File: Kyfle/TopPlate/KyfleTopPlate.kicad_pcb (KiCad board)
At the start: 2 copper layers, 160.8 x 138.4 mm, 39 parts, among them SW2 KEY_SWITCH, SW2 PRO MICRO

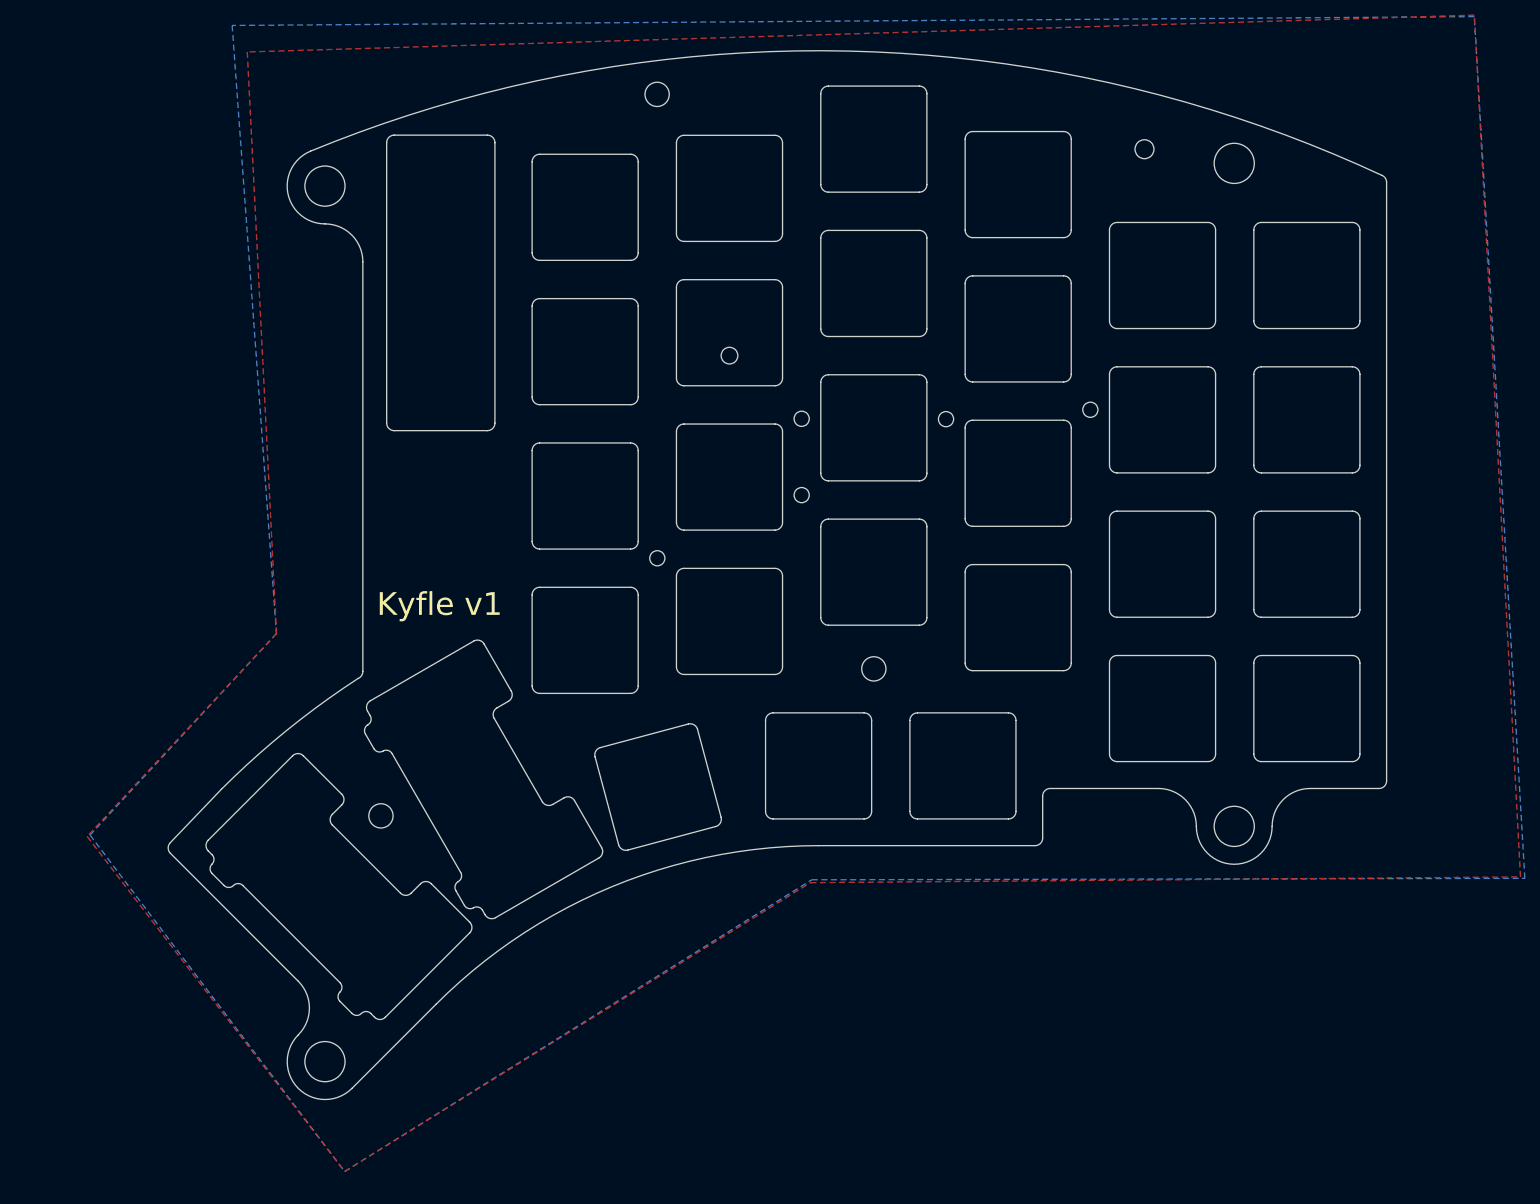
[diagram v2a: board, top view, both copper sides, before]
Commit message: Experimentation with different fastening solutions. Not great.
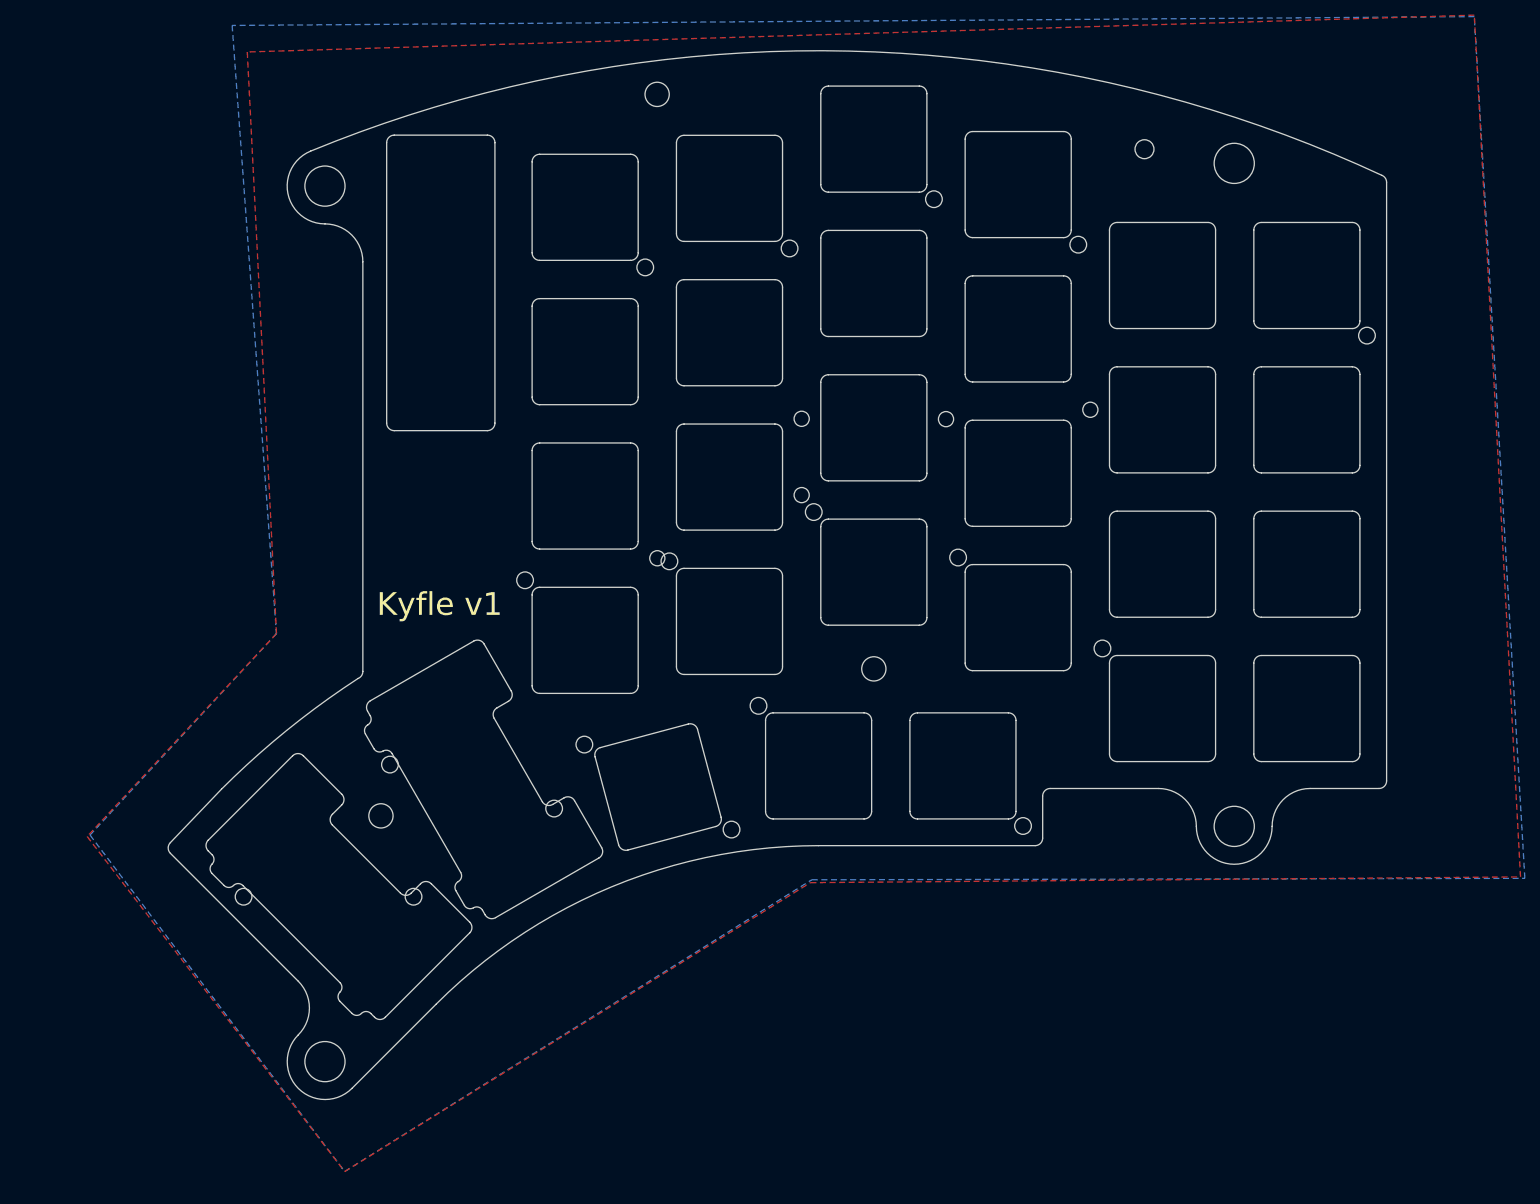
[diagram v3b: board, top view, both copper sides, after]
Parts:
- removed the REF** at (150.0, 64.0)
- added REF**: MountingHole_2.2mm_M2_ISO14580, SofleChocTop:M2_with_washer, F.Cu at (153.8, 110.2)
- added REF**: MountingHole_2.2mm_M2_ISO14580, SofleChocTop:M2_with_washer, F.Cu at (177.0, 43.3)
- added REF**: MountingHole_2.2mm_M2_ISO14580, SofleChocTop:M2_with_washer, F.Cu at (85.9, 135.4)
- added REF**: MountingHole_2.2mm_M2_ISO14580, SofleChocTop:M2_with_washer, F.Cu at (161.1, 84.6)
- added REF**: MountingHole_2.2mm_M2_ISO14580, SofleChocTop:M2_with_washer, F.Cu at (188.7, 126.0)
- added REF**: MountingHole_2.2mm_M2_ISO14580, SofleChocTop:M2_with_washer, F.Cu at (157.9, 49.8)
- added REF**: MountingHole_2.2mm_M2_ISO14580, SofleChocTop:M2_with_washer, F.Cu at (142.1, 91.1)
- added REF**: MountingHole_2.2mm_M2_ISO14580, SofleChocTop:M2_with_washer, F.Cu at (105.2, 117.9)
- added REF**: MountingHole_2.2mm_M2_ISO14580, SofleChocTop:M2_with_washer, F.Cu at (138.9, 52.3)
- added REF**: MountingHole_2.2mm_M2_ISO14580, SofleChocTop:M2_with_washer, F.Cu at (130.8, 115.3)
- added REF**: MountingHole_2.2mm_M2_ISO14580, SofleChocTop:M2_with_washer, F.Cu at (108.3, 135.4)
- added REF**: MountingHole_2.2mm_M2_ISO14580, SofleChocTop:M2_with_washer, F.Cu at (180.2, 90.6)
- added REF**: MountingHole_2.2mm_M2_ISO14580, SofleChocTop:M2_with_washer, F.Cu at (234.1, 61.3)
- added REF**: MountingHole_2.2mm_M2_ISO14580, SofleChocTop:M2_with_washer, F.Cu at (126.9, 123.7)
- added REF**: MountingHole_2.2mm_M2_ISO14580, SofleChocTop:M2_with_washer, F.Cu at (199.2, 102.6)
- added REF**: MountingHole_2.2mm_M2_ISO14580, SofleChocTop:M2_with_washer, F.Cu at (150.3, 126.5)
- added REF**: MountingHole_2.2mm_M2_ISO14580, SofleChocTop:M2_with_washer, F.Cu at (123.0, 93.6)
- added REF**: MountingHole_2.2mm_M2_ISO14580, SofleChocTop:M2_with_washer, F.Cu at (196.0, 49.3)

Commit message: Settled on a solution to fix the PCB
It will be hold by the bottom plate only.
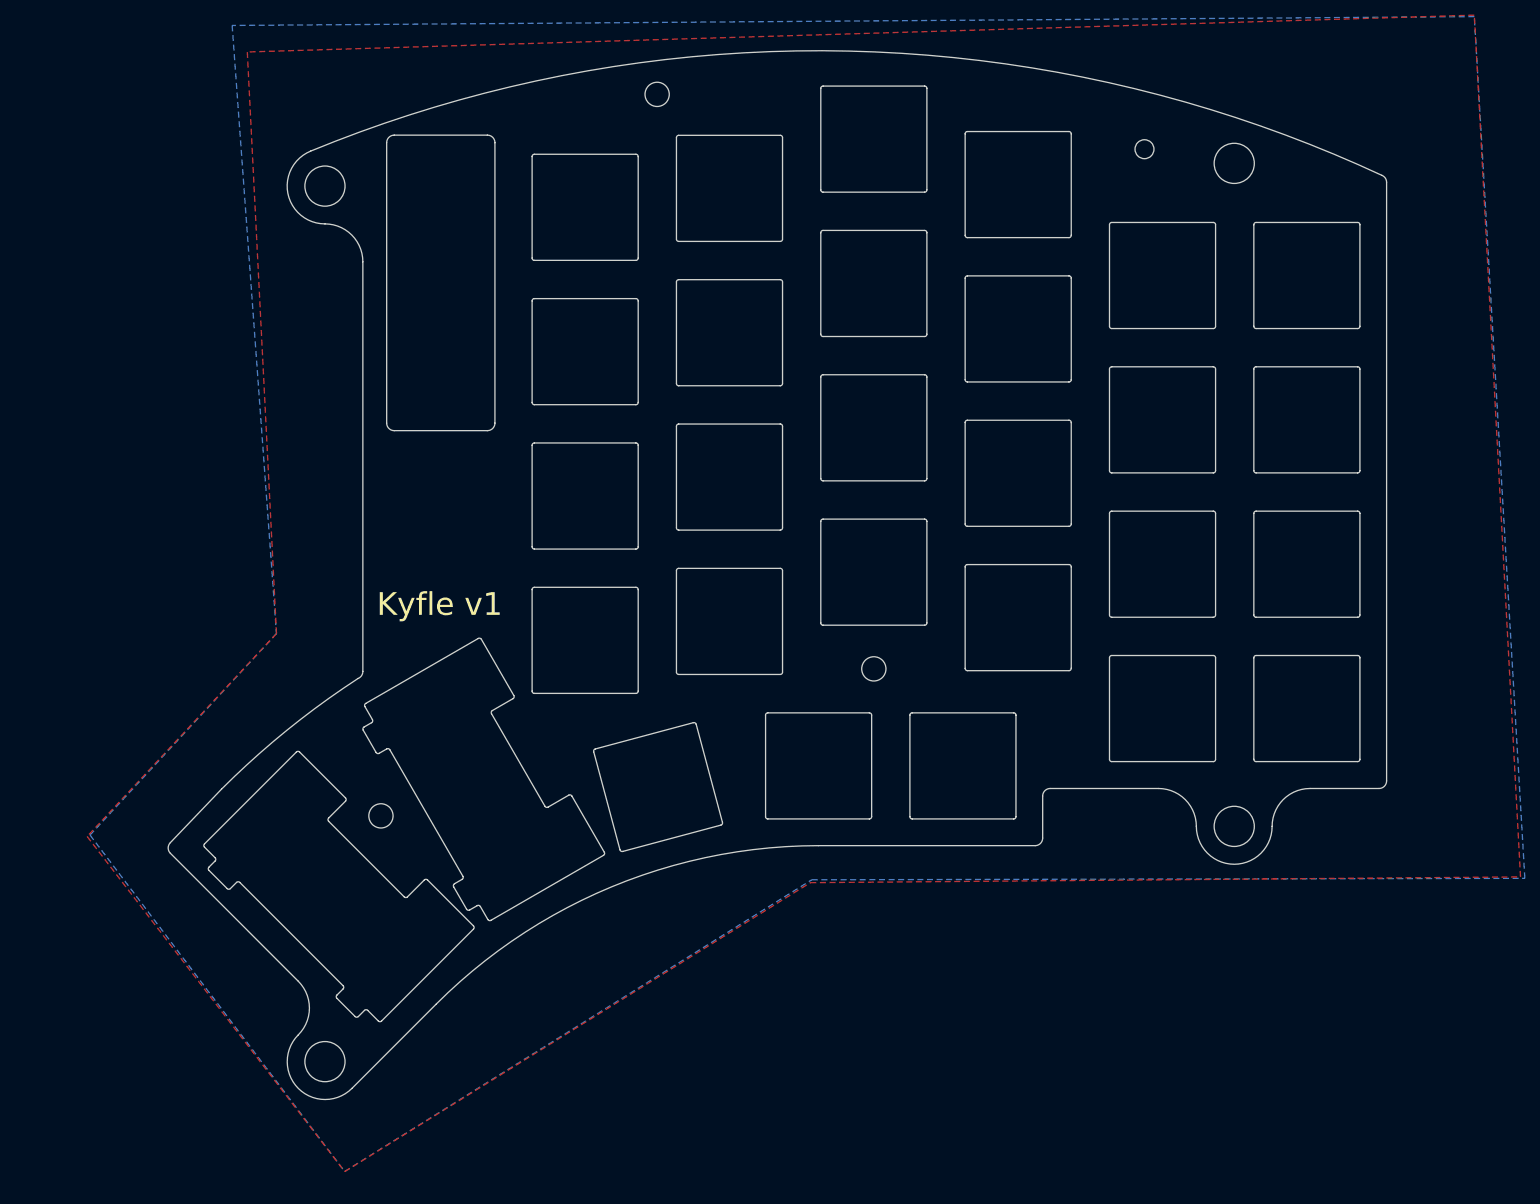
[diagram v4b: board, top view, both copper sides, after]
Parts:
- removed the REF** at (153.8, 110.2)
- removed the REF** at (177.0, 43.3)
- removed the REF** at (85.9, 135.4)
- removed the REF** at (161.1, 84.6)
- removed the REF** at (188.7, 126.0)
- removed the REF** at (157.9, 49.8)
- removed the REF** at (142.1, 91.1)
- removed the REF** at (105.2, 117.9)
- removed the REF** at (138.9, 52.3)
- removed the REF** at (130.8, 115.3)
- removed the REF** at (108.3, 135.4)
- removed the REF** at (180.2, 90.6)
- removed the REF** at (234.1, 61.3)
- removed the REF** at (126.9, 123.7)
- removed the REF** at (199.2, 102.6)
- removed the REF** at (150.3, 126.5)
- removed the REF** at (123.0, 93.6)
- removed the REF** at (196.0, 49.3)
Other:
- outline, holes or cut-outs redrawn

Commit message: Fixuturing solution for the pro micro board
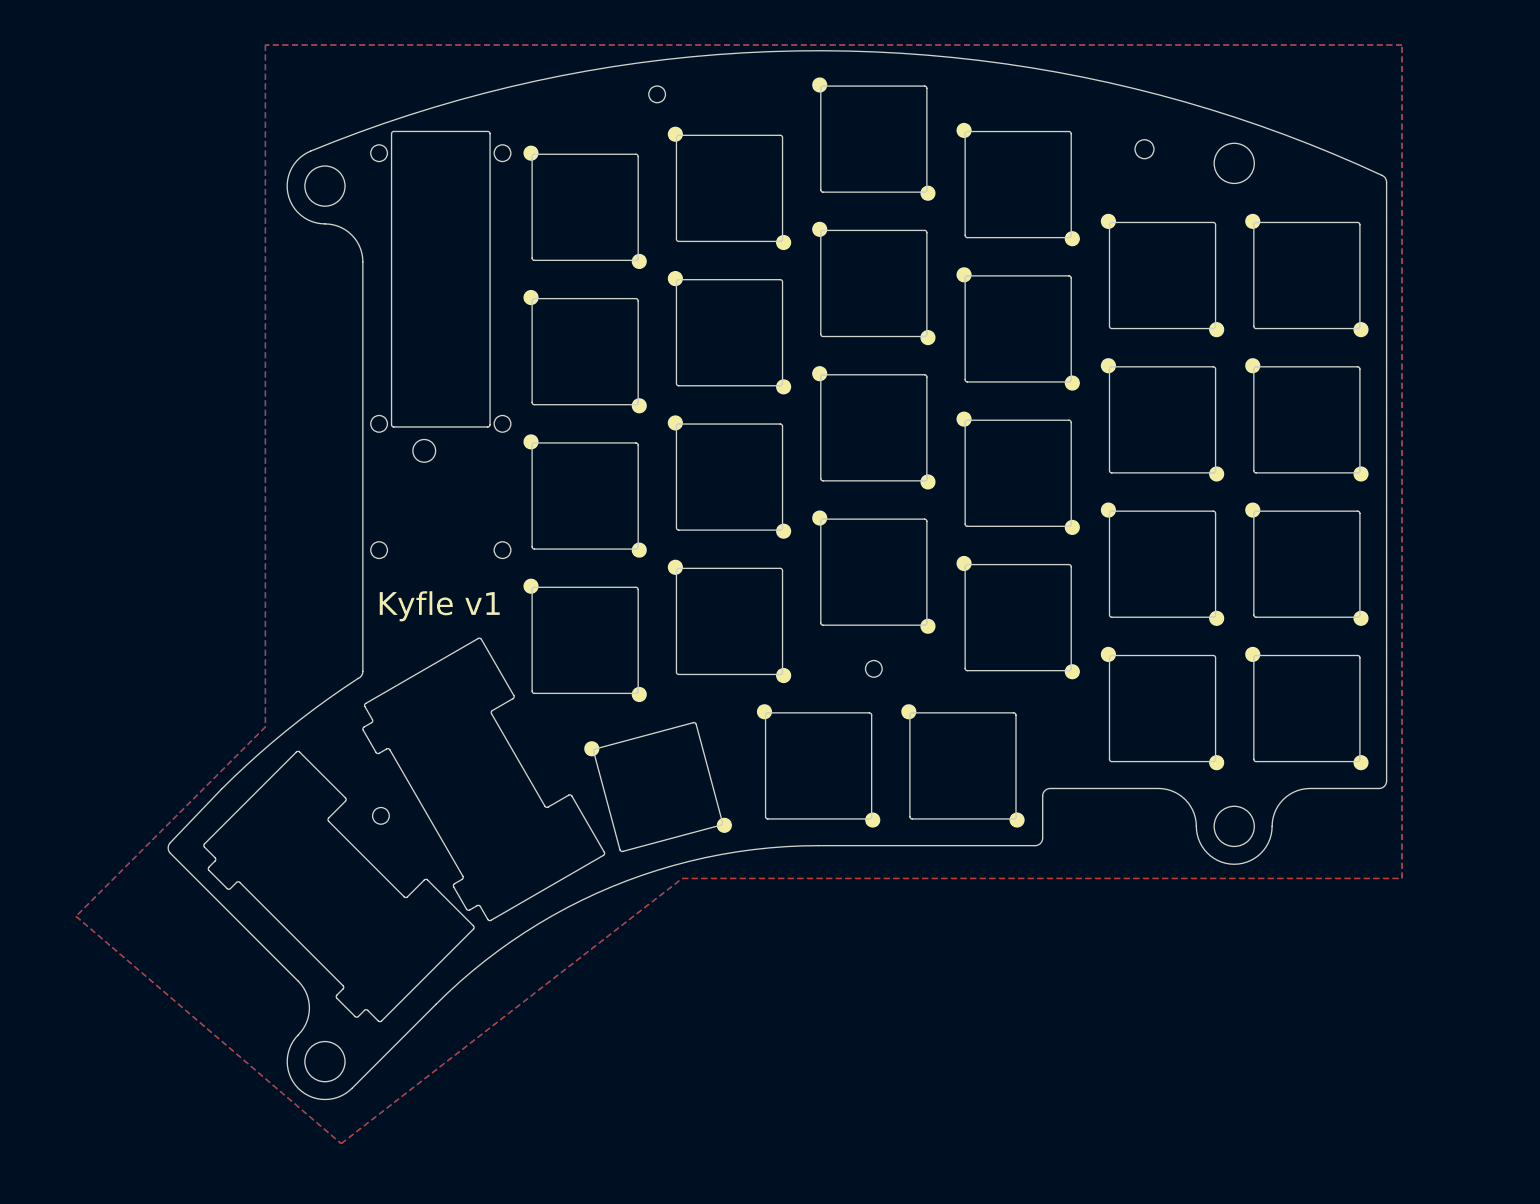
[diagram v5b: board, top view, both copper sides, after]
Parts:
- added REF**: MountingHole_2.2mm_M2_ISO14580, SofleChocTop:M2_with_washer, F.Cu at (103.8, 37.3)
- added REF**: MountingHole_2.2mm_M2_ISO14580, SofleChocTop:M2_with_washer, F.Cu at (120.0, 89.6)
- added REF**: MountingHole_2.2mm_M2_ISO14580, SofleChocTop:M2_with_washer, F.Cu at (103.8, 89.6)
- added REF**: MountingHole_2.2mm_M2_ISO14580, SofleChocTop:M2_with_washer, F.Cu at (103.8, 73.0)
- added REF**: MountingHole_2.2mm_M2_ISO14580, SofleChocTop:M2_with_washer, F.Cu at (120.0, 73.0)
- added REF**: MountingHole_2.2mm_M2_ISO14580, SofleChocTop:M2_with_washer, F.Cu at (120.0, 37.3)
- REF** (x4): value MountingHole_5.3mm_M5_ISO14580 -> MountingHole_2.2mm_M2_ISO14580; footprint MountingHole:MountingHole_5.3mm_M5_ISO14580 -> SofleChocTop:M5_with_washer
- SW2 (x2): footprint SofleChocTop:SW_Hole_2u -> SofleChocTop:SU120_RGB_SW_2u_Top
- SW2 (x27): footprint SofleChocTop:SW_Hole -> SofleChocTop:SU120_RGB_SW_Top
- SW2: footprint SofleChocTop:SU120_ProMicro -> SofleChocTop:SU120_ProMicro_Top
- TH3, TH7 (x2): footprint MountingHole:MountingHole_3.2mm_M3_ISO14580 -> SofleChocTop:M2_with_washer
